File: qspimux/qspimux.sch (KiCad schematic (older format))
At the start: 9 parts, among them J101 Conn_02x05_Odd_Even, J102 Conn_02x04_Odd_Even, J103 Conn_02x04_Odd_Even, Q101 PMV50XP, Q102 PMV50XP, U101 TS3A27518ERTWR

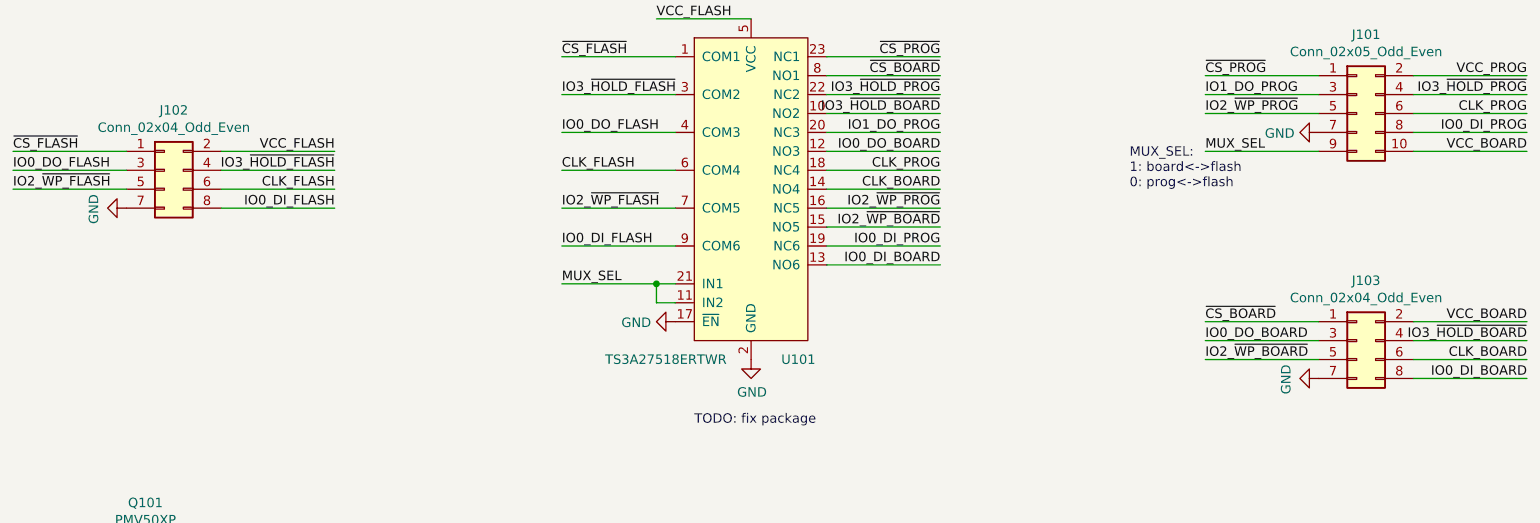
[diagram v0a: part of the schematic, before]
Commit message: fix mirrored footprints in qspimux design
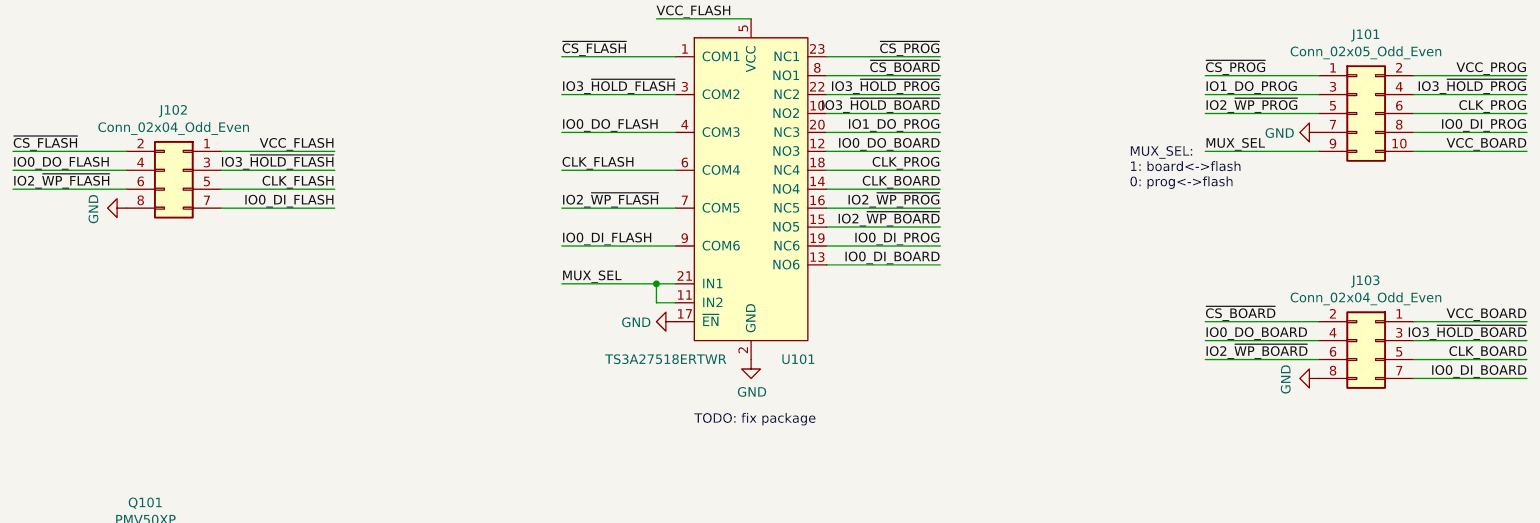
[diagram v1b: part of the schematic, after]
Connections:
- net CLK_BOARD: now also J103.5 (Pin_5); no longer J103.6 (Pin_6)
- net CLK_FLASH: now also J102.5 (Pin_5); no longer J102.6 (Pin_6)
- net GND: now also J102.8 (Pin_8), J103.8 (Pin_8); no longer J102.7 (Pin_7), J103.7 (Pin_7)
- net IO0_DI_BOARD: now also J103.7 (Pin_7); no longer J103.8 (Pin_8)
- net IO0_DI_FLASH: now also J102.7 (Pin_7); no longer J102.8 (Pin_8)
- net IO0_DO_BOARD: now also J103.4 (Pin_4); no longer J103.3 (Pin_3)
- net IO0_DO_FLASH: now also J102.4 (Pin_4); no longer J102.3 (Pin_3)
- net IO2_~WP_BOARD: now also J103.6 (Pin_6); no longer J103.5 (Pin_5)
- net IO2_~WP_FLASH: now also J102.6 (Pin_6); no longer J102.5 (Pin_5)
- net IO3_~HOLD_BOARD: now also J103.3 (Pin_3); no longer J103.4 (Pin_4)
- net IO3_~HOLD_FLASH: now also J102.3 (Pin_3); no longer J102.4 (Pin_4)
- net VCC_BOARD: now also J103.1 (Pin_1); no longer J103.2 (Pin_2)
- net VCC_FLASH: now also J102.1 (Pin_1); no longer J102.2 (Pin_2)
- net ~CS_BOARD: now also J103.2 (Pin_2); no longer J103.1 (Pin_1)
- net ~CS_FLASH: now also J102.2 (Pin_2); no longer J102.1 (Pin_1)
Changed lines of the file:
@@
 L Connector_Generic:Conn_02x04_Odd_Even J102
 U 1 1 5B60D78F
-P 2200 3300
-F 0 "J102" H 2250 3617 50  0000 C CNN
-F 1 "Conn_02x04_Odd_Even" H 2250 3526 50  0000 C CNN
-F 2 "Connector_PinSocket_1.27mm:PinSocket_2x04_P1.27mm_Vertical_SMD" H 2200 3300 50  0001 C CNN
-F 3 "~" H 2200 3300 50  0001 C CNN
-	1    2200 3300
-	1    0    0    -1
+P 2300 3300
+F 0 "J102" H 2350 3617 50  0000 C CNN
+F 1 "Conn_02x04_Odd_Even" H 2350 3526 50  0000 C CNN
+F 2 "Connector_PinSocket_1.27mm:PinSocket_2x04_P1.27mm_Vertical_SMD" H 2300 3300 50  0001 C CNN
+F 3 "~" H 2300 3300 50  0001 C CNN
+	1    2300 3300
+	-1   0    0    -1
 $EndComp
 $Comp
 L Connector_Generic:Conn_02x04_Odd_Even J103
 U 1 1 5B60D7DE
-P 8500 4200
-F 0 "J103" H 8550 4517 50  0000 C CNN
-F 1 "Conn_02x04_Odd_Even" H 8550 4426 50  0000 C CNN
-F 2 "Connector_PinHeader_1.27mm:PinHeader_2x04_P1.27mm_Vertical_SMD" H 8500 4200 50  0001 C CNN
-F 3 "~" H 8500 4200 50  0001 C CNN
-	1    8500 4200
-	1    0    0    -1
+P 8600 4200
+F 0 "J103" H 8650 4517 50  0000 C CNN
+F 1 "Conn_02x04_Odd_Even" H 8650 4426 50  0000 C CNN
+F 2 "Connector_PinHeader_1.27mm:PinHeader_2x04_P1.27mm_Vertical_SMD" H 8600 4200 50  0001 C CNN
+F 3 "~" H 8600 4200 50  0001 C CNN
+	1    8600 4200
+	-1   0    0    -1
 $EndComp
 Wire Wire Line

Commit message: fix power supply circuitry
The old version was lacking reverse current protection on Q101.
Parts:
- removed Q101, Q102: PMV50XP, Package_TO_SOT_SMD:SOT-23, symbol Transistor_FET:PMV50XP
- removed R102: 4k7, Resistor_SMD:R_0402_1005Metric, symbol Device:R
- added C102, C103: 100n, Capacitor_SMD:C_0402_1005Metric, symbol Device:C
- added U102, U103: MAX40200AUK, Package_TO_SOT_SMD:SOT-23-5, symbol Power_Management:MAX40200AUK
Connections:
- wire segments 56 -> 61
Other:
- note removed: "add 0 ohm resistor in vcc board line to q102?"
- moved on the sheet: C101
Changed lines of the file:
@@
 IO3_~HOLD_BOARD
 Wire Wire Line
-	2800 5300 2300 5300
-Text Label 2800 5300 2    50   ~ 0
-VCC_FLASH
-Wire Wire Line
-	1400 6100 1900 6100
-Text Label 1400 6100 0    50   ~ 0
+	3100 5300 2600 5300
+Text Label 3100 5300 2    50   ~ 0
+VCC_FLASH
+Wire Wire Line
+	1500 6300 1900 6300
+Text Label 1500 6300 0    50   ~ 0
 VCC_PROG
 Wire Wire Line
-	1400 5300 1900 5300
-Text Label 1400 5300 0    50   ~ 0
+	4700 6200 5200 6200
+Text Label 4700 6200 0    50   ~ 0
 VCC_BOARD
 Text Label 4300 3900 0    50   ~ 0
@@
 L Device:C C101
 U 1 1 5B6EA565
-P 4300 6150
-F 0 "C101" H 4415 6196 50  0000 L CNN
-F 1 "100n" H 4415 6105 50  0000 L CNN
-F 2 "Capacitor_SMD:C_0402_1005Metric" H 4338 6000 50  0001 C CNN
-F 3 "~" H 4300 6150 50  0001 C CNN
-	1    4300 6150
-	1    0    0    -1
-$EndComp
-Wire Wire Line
-	3800 6000 4300 6000
-Text Label 3800 6000 0    50   ~ 0
+P 5200 5550
+F 0 "C101" H 5315 5596 50  0000 L CNN
+F 1 "100n" H 5315 5505 50  0000 L CNN
+F 2 "Capacitor_SMD:C_0402_1005Metric" H 5238 5400 50  0001 C CNN
+F 3 "~" H 5200 5550 50  0001 C CNN
+	1    5200 5550
+	1    0    0    -1
+$EndComp
+Wire Wire Line
+	4700 5400 5200 5400
+Text Label 4700 5400 0    50   ~ 0
 VCC_FLASH
 $Comp
 L power:GND #PWR0107
 U 1 1 5B6ED428
-P 4300 6300
-F 0 "#PWR0107" H 4300 6050 50  0001 C CNN
-F 1 "GND" H 4305 6127 50  0000 C CNN
-F 2 "" H 4300 6300 50  0001 C CNN
-F 3 "" H 4300 6300 50  0001 C CNN
-	1    4300 6300
-	1    0    0    -1
-$EndComp
-$Comp
-L Transistor_FET:PMV50XP Q101
-U 1 1 5B7249B6
-P 2100 5400
-F 0 "Q101" V 2443 5400 50  0000 C CNN
-F 1 "PMV50XP" V 2352 5400 50  0000 C CNN
-F 2 "Package_TO_SOT_SMD:SOT-23" H 2300 5325 50  0001 L CIN
-F 3 "" H 2100 5400 50  0001 L CNN
-	1    2100 5400
-	0    -1   -1   0
+P 5200 5700
+F 0 "#PWR0107" H 5200 5450 50  0001 C CNN
+F 1 "GND" H 5205 5527 50  0000 C CNN
+F 2 "" H 5200 5700 50  0001 C CNN
+F 3 "" H 5200 5700 50  0001 C CNN
+	1    5200 5700
+	1    0    0    -1
 $EndComp
 $Comp
 L power:GND #PWR0106
 U 1 1 5B72A64D
-P 2100 5600
-F 0 "#PWR0106" H 2100 5350 50  0001 C CNN
-F 1 "GND" H 2105 5427 50  0000 C CNN
-F 2 "" H 2100 5600 50  0001 C CNN
-F 3 "" H 2100 5600 50  0001 C CNN
-	1    2100 5600
-	1    0    0    -1
-$EndComp
-$Comp
-L Transistor_FET:PMV50XP Q102
-U 1 1 5B72A666
-P 2100 6200
-F 0 "Q102" V 2443 6200 50  0000 C CNN
-F 1 "PMV50XP" V 2352 6200 50  0000 C CNN
-F 2 "Package_TO_SOT_SMD:SOT-23" H 2300 6125 50  0001 L CIN
-F 3 "" H 2100 6200 50  0001 L CNN
-	1    2100 6200
-	0    -1   -1   0
-$EndComp
-$Comp
-L power:GND #PWR0108
+P 2300 5700
+F 0 "#PWR0106" H 2300 5450 50  0001 C CNN
+F 1 "GND" H 2305 5527 50  0000 C CNN
+F 2 "" H 2300 5700 50  0001 C CNN
+F 3 "" H 2300 5700 50  0001 C CNN
+	1    2300 5700
+	1    0    0    -1
+$EndComp
+$Comp
+L power:GND #PWR0109
 U 1 1 5B72A698
-P 2100 6900
-F 0 "#PWR0108" H 2100 6650 50  0001 C CNN
-F 1 "GND" H 2105 6727 50  0000 C CNN
-F 2 "" H 2100 6900 50  0001 C CNN
-F 3 "" H 2100 6900 50  0001 C CNN
-	1    2100 6900
-	1    0    0    -1
-$EndComp
-Wire Wire Line
-	2800 6100 2300 6100
-Text Label 2800 6100 2    50   ~ 0
-VCC_FLASH
-$Comp
-L Device:R R102
-U 1 1 5B7307D7
-P 2100 6750
-F 0 "R102" H 2170 6796 50  0000 L CNN
-F 1 "4k7" H 2170 6705 50  0000 L CNN
-F 2 "Resistor_SMD:R_0402_1005Metric" V 2030 6750 50  0001 C CNN
-F 3 "~" H 2100 6750 50  0001 C CNN
-	1    2100 6750
-	1    0    0    -1
-$EndComp
-Wire Wire Line
-	1400 6500 2100 6500
-Wire Wire Line
-	2100 6400 2100 6500
-Wire Wire Line
-	2100 6600 2100 6500
-Connection ~ 2100 6500
-Text Label 1400 6500 0    50   ~ 0
-VCC_BOARD
-Text Notes 1400 6400 0    50   ~ 0
-add 0 ohm resistor in vcc board line to q102?
+P 2300 6700
+F 0 "#PWR0109" H 2300 6450 50  0001 C CNN
+F 1 "GND" H 2305 6527 50  0000 C CNN
+F 2 "" H 2300 6700 50  0001 C CNN
+F 3 "" H 2300 6700 50  0001 C CNN
+	1    2300 6700
+	1    0    0    -1
+$EndComp
+Wire Wire Line
+	3100 6300 2600 6300
+Text Label 3100 6300 2    50   ~ 0
+VCC_FLASH
 Text Notes 8000 2100 0    50   ~ 0
 connect flash to board if\nproggrammer is unconnected
 Text Notes 1100 1400 0    50   ~ 0
 assumption: VCC_BOARD is about the same as VCC_PROG an both are between 1.8V and 3.3v
+$Comp
+L Power_Management:MAX40200AUK U102
+U 1 1 5B781CF7
+P 2300 5500
+F 0 "U102" H 2300 5965 50  0000 C CNN
+F 1 "MAX40200AUK" H 2300 5874 50  0000 C CNN
+F 2 "Package_TO_SOT_SMD:SOT-23-5" H 2300 5500 50  0001 C CNN
+F 3 "" H 2300 5500 50  0001 C CNN
+	1    2300 5500
+	1    0    0    -1
+$EndComp
+$Comp
+L Power_Management:MAX40200AUK U103
+U 1 1 5B781D59
+P 2300 6500
+F 0 "U103" H 2300 6965 50  0000 C CNN
+F 1 "MAX40200AUK" H 2300 6874 50  0000 C CNN
+F 2 "Package_TO_SOT_SMD:SOT-23-5" H 2300 6500 50  0001 C CNN
+F 3 "" H 2300 6500 50  0001 C CNN
+	1    2300 6500
+	1    0    0    -1
+$EndComp
+$Comp
+L power:PWR_FLAG #FLG0103
+U 1 1 5B7A6FC6
+P 3700 7000
+F 0 "#FLG0103" H 3700 7075 50  0001 C CNN
+F 1 "PWR_FLAG" H 3700 7174 50  0000 C CNN
+F 2 "" H 3700 7000 50  0001 C CNN
+F 3 "~" H 3700 7000 50  0001 C CNN
+	1    3700 7000
+	1    0    0    -1
+$EndComp
+$Comp
+L power:GND #PWR0110
+U 1 1 5B7A708C
+P 3700 7000
+F 0 "#PWR0110" H 3700 6750 50  0001 C CNN
+F 1 "GND" H 3705 6827 50  0000 C CNN
+F 2 "" H 3700 7000 50  0001 C CNN
+F 3 "" H 3700 7000 50  0001 C CNN
+	1    3700 7000
+	1    0    0    -1
+$EndComp
+$Comp
+L power:PWR_FLAG #FLG0102
+U 1 1 5B7A70A9
+P 5200 6200
+F 0 "#FLG0102" H 5200 6275 50  0001 C CNN
+F 1 "PWR_FLAG" H 5200 6374 50  0000 C CNN
+F 2 "" H 5200 6200 50  0001 C CNN
+F 3 "~" H 5200 6200 50  0001 C CNN
+	1    5200 6200
+	1    0    0    -1
+$EndComp
+$Comp
+L power:PWR_FLAG #FLG0104
+U 1 1 5B7AA686
+P 5200 7000
+F 0 "#FLG0104" H 5200 7075 50  0001 C CNN
+F 1 "PWR_FLAG" H 5200 7174 50  0000 C CNN
+F 2 "" H 5200 7000 50  0001 C CNN
+F 3 "~" H 5200 7000 50  0001 C CNN
+	1    5200 7000
+	1    0    0    -1
+$EndComp
+Wire Wire Line
+	1500 5300 1900 5300
+Text Label 1500 5300 0    50   ~ 0
+VCC_BOARD
+$Comp
+L power:PWR_FLAG #FLG0101
+U 1 1 5B7AC3D7
+P 5200 5400
+F 0 "#FLG0101" H 5200 5475 50  0001 C CNN
+F 1 "PWR_FLAG" H 5200 5574 50  0000 C CNN
+F 2 "" H 5200 5400 50  0001 C CNN
+F 3 "~" H 5200 5400 50  0001 C CNN
+	1    5200 5400
+	1    0    0    -1
+$EndComp
+Wire Wire Line
+	4700 7000 5200 7000
+Text Label 4700 7000 0    50   ~ 0
+VCC_PROG
+Wire Wire Line
+	2000 5400 1900 5400
+Wire Wire Line
+	1900 5400 1900 5300
+Connection ~ 1900 5300
+Wire Wire Line
+	1900 5300 2000 5300
+Wire Wire Line
+	2000 6400 1900 6400
+Wire Wire Line
+	1900 6400 1900 6300
+Connection ~ 1900 6300
+Wire Wire Line
+	1900 6300 2000 6300
+Connection ~ 5200 5400
+$Comp
+L Device:C C103
+U 1 1 5B7BD066
+P 5200 7150
+F 0 "C103" H 5315 7196 50  0000 L CNN
+F 1 "100n" H 5315 7105 50  0000 L CNN
+F 2 "Capacitor_SMD:C_0402_1005Metric" H 5238 7000 50  0001 C CNN
+F 3 "~" H 5200 7150 50  0001 C CNN
+	1    5200 7150
+	1    0    0    -1
+$EndComp
+$Comp
+L power:GND #PWR0111
+U 1 1 5B7BD06C
+P 5200 7300
+F 0 "#PWR0111" H 5200 7050 50  0001 C CNN
+F 1 "GND" H 5205 7127 50  0000 C CNN
+F 2 "" H 5200 7300 50  0001 C CNN
+F 3 "" H 5200 7300 50  0001 C CNN
+	1    5200 7300
+	1    0    0    -1
+$EndComp
+Connection ~ 5200 7000
+$Comp
+L Device:C C102
+U 1 1 5B7C2CDA
+P 5200 6350
+F 0 "C102" H 5315 6396 50  0000 L CNN
+F 1 "100n" H 5315 6305 50  0000 L CNN
+F 2 "Capacitor_SMD:C_0402_1005Metric" H 5238 6200 50  0001 C CNN
+F 3 "~" H 5200 6350 50  0001 C CNN
+	1    5200 6350
+	1    0    0    -1
+$EndComp
+$Comp
+L power:GND #PWR0108
+U 1 1 5B7C2CE0
+P 5200 6500
+F 0 "#PWR0108" H 5200 6250 50  0001 C CNN
+F 1 "GND" H 5205 6327 50  0000 C CNN
+F 2 "" H 5200 6500 50  0001 C CNN
+F 3 "" H 5200 6500 50  0001 C CNN
+	1    5200 6500
+	1    0    0    -1
+$EndComp
+Connection ~ 5200 6200
 $EndSCHEMATC

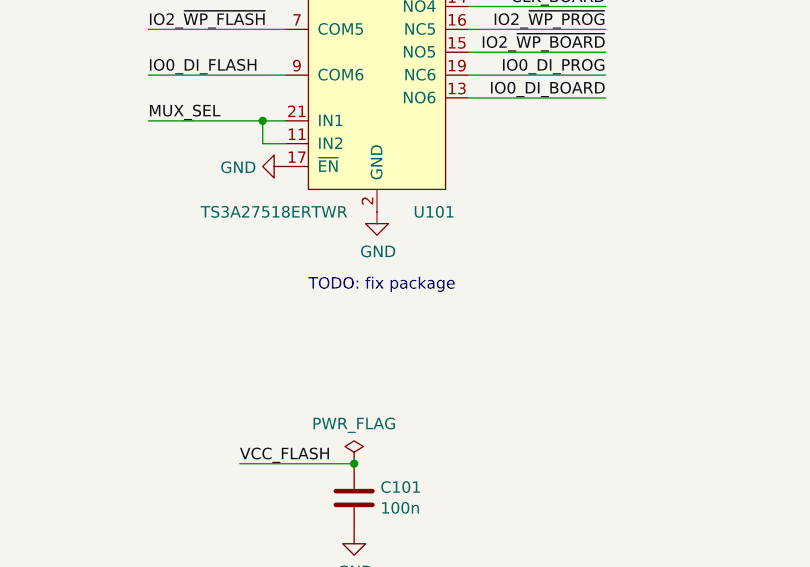
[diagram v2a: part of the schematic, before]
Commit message: move layout-related TODO to layout file
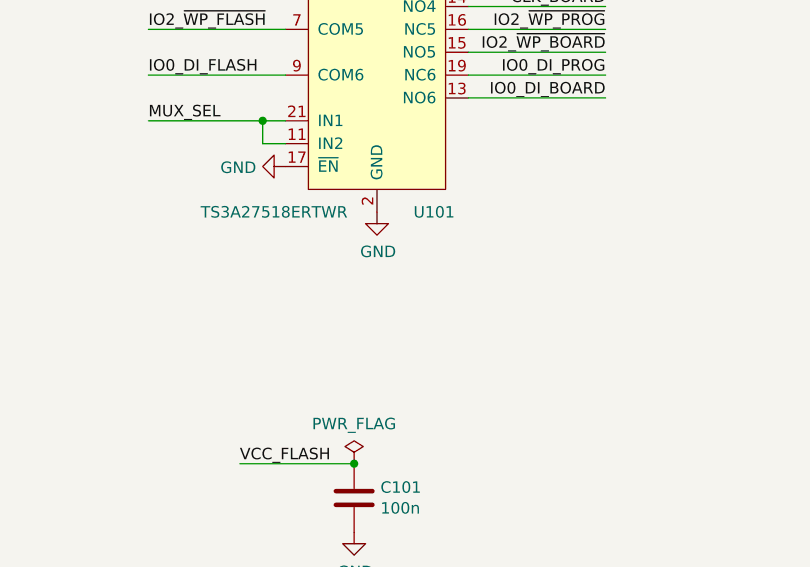
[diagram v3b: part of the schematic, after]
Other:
- note removed: "TODO: fix package"
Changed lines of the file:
@@
 	1    0    0    -1
 $EndComp
-Text Notes 5000 4650 0    50   ~ 0
-TODO: fix package
 Wire Wire Line
 	4900 4000 4800 4000

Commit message: fix footprint of TS3A27518ERTWR
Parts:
- U101: footprint Package_DFN_QFN:QFN-24-1EP_4x4mm_P0.5mm_EP2.6x2.6mm -> Package_DFN_QFN:QFN-24_1EP_3.9x3.9mm_Pitch0.5mm
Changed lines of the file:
@@
 F 0 "U101" H 5550 2300 50  0000 C CNN
 F 1 "TS3A27518ERTWR" H 4850 2300 50  0000 C CNN
-F 2 "Package_DFN_QFN:QFN-24-1EP_4x4mm_P0.5mm_EP2.6x2.6mm" H 5350 1250 50  0001 C CNN
+F 2 "Package_DFN_QFN:QFN-24_1EP_3.9x3.9mm_Pitch0.5mm" H 5350 1250 50  0001 C CNN
 F 3 "" H 5350 1250 50  0001 C CNN
 	1    5300 3300

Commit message: qspimux: update project to use newly included symbols/footprints
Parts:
- U101: footprint Package_DFN_QFN:QFN-24_1EP_3.9x3.9mm_Pitch0.5mm -> qspimux-footprints:QFN-24_1EP_3.9x3.9mm_Pitch0.5mm
- U102, U103: symbol Power_Management:MAX40200AUK -> MAX40200:MAX40200AUK
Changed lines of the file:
@@
 EESchema Schematic File Version 4
 LIBS:qspimux-cache
-EELAYER 26 0
+EELAYER 29 0
 EELAYER END
 $Descr A4 11693 8268
@@
 F 0 "U101" H 5550 2300 50  0000 C CNN
 F 1 "TS3A27518ERTWR" H 4850 2300 50  0000 C CNN
-F 2 "Package_DFN_QFN:QFN-24_1EP_3.9x3.9mm_Pitch0.5mm" H 5350 1250 50  0001 C CNN
+F 2 "qspimux-footprints:QFN-24_1EP_3.9x3.9mm_Pitch0.5mm" H 5350 1250 50  0001 C CNN
 F 3 "" H 5350 1250 50  0001 C CNN
 	1    5300 3300
@@
 assumption: VCC_BOARD is about the same as VCC_PROG an both are between 1.8V and 3.3v
 $Comp
-L Power_Management:MAX40200AUK U102
+L MAX40200:MAX40200AUK U102
 U 1 1 5B781CF7
 P 2300 5500
@@
 $EndComp
 $Comp
-L Power_Management:MAX40200AUK U103
+L MAX40200:MAX40200AUK U103
 U 1 1 5B781D59
 P 2300 6500

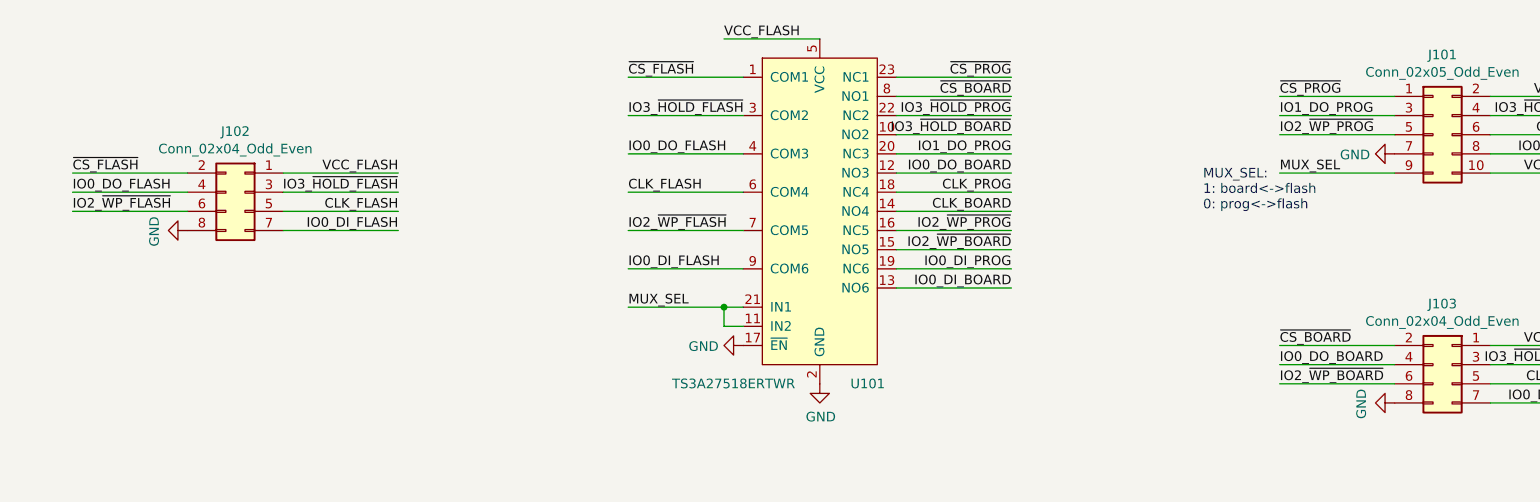
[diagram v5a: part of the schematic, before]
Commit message: qspimux: fix remaining net name bug
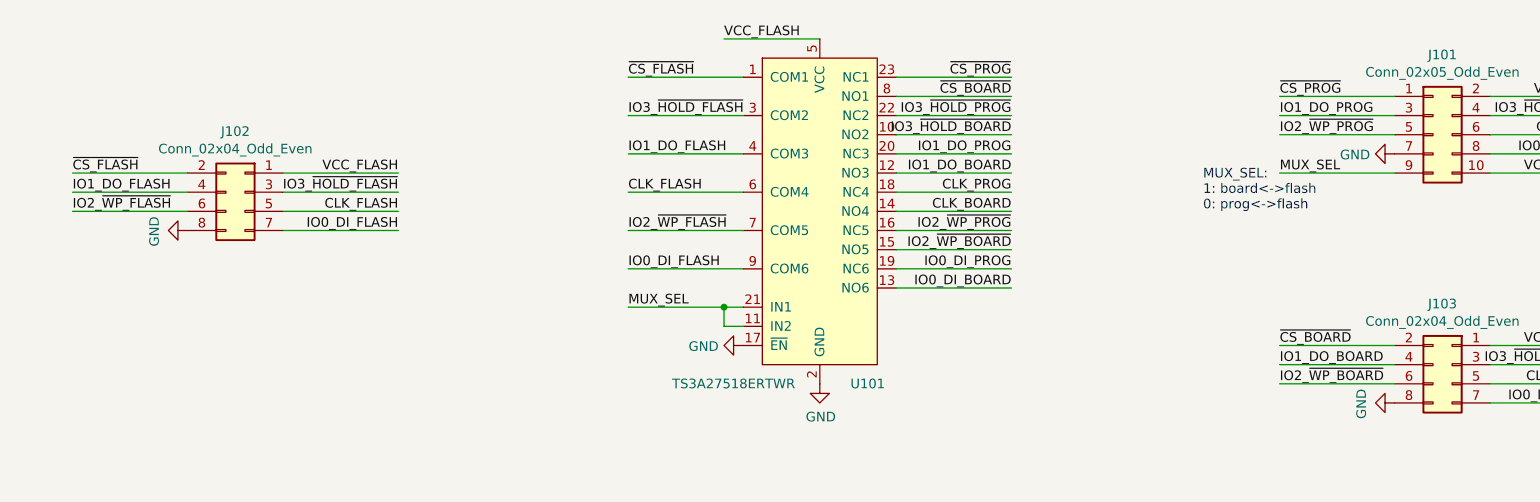
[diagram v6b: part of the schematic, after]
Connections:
- net IO0_DO_BOARD renamed IO1_DO_BOARD
- net IO0_DO_FLASH renamed IO1_DO_FLASH
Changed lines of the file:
@@
 ~CS_FLASH
 Text Label 1400 3300 0    50   ~ 0
-IO0_DO_FLASH
+IO1_DO_FLASH
 Text Label 1400 3400 0    50   ~ 0
 IO2_~WP_FLASH
@@
 ~CS_BOARD
 Text Label 7700 4200 0    50   ~ 0
-IO0_DO_BOARD
+IO1_DO_BOARD
 Text Label 7700 4300 0    50   ~ 0
 IO2_~WP_BOARD
@@
 ~CS_FLASH
 Text Label 4300 3100 0    50   ~ 0
-IO0_DO_FLASH
+IO1_DO_FLASH
 Text Label 4300 3500 0    50   ~ 0
 IO2_~WP_FLASH
@@
 ~CS_BOARD
 Text Label 6300 3200 2    50   ~ 0
-IO0_DO_BOARD
+IO1_DO_BOARD
 Text Label 6300 3600 2    50   ~ 0
 IO2_~WP_BOARD
